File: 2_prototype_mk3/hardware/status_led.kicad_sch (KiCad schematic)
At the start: 2 parts

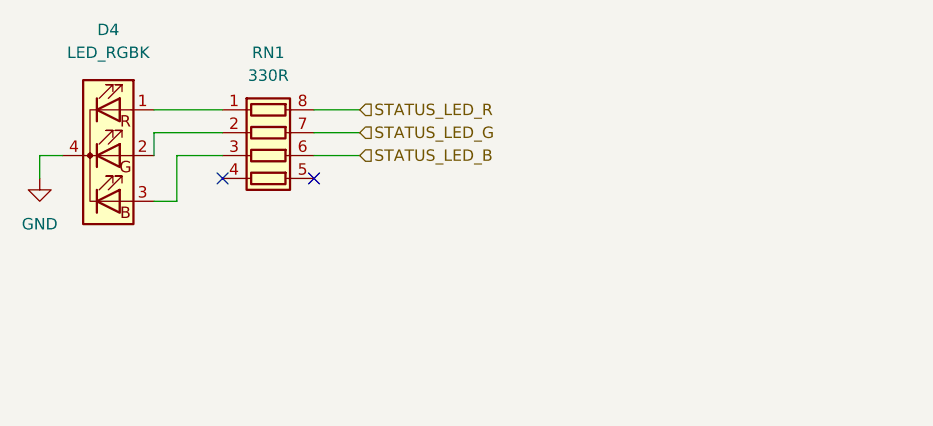
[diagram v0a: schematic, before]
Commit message: Add net classes for power
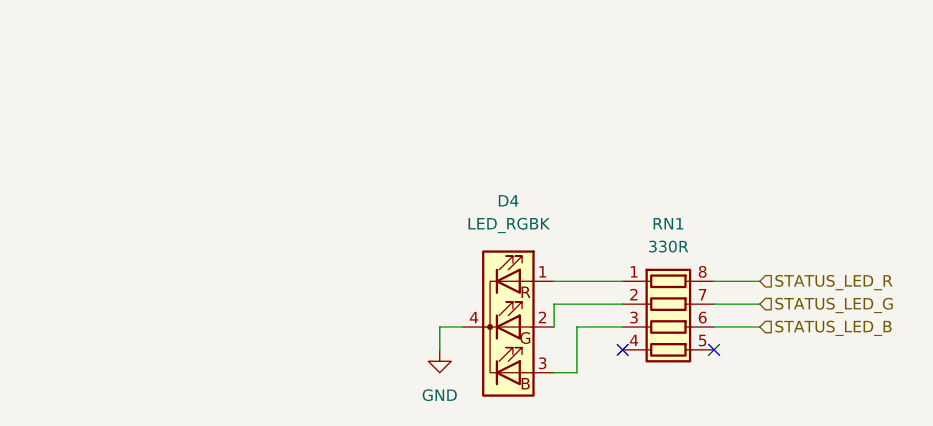
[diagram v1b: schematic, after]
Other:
- title: Status LED -> (none)
- moved on the sheet: D4, RN1
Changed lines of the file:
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@@
 	(generator "eeschema")
 	(generator_version "9.0")
-	(paper "A5")
-	(title_block
-		(title "Status LED")
-	)
+	(paper "A4")
 	(no_connect
-		(at 100.33 73.66)
+		(at 144.78 92.71)
 	)
 	(no_connect
-		(at 110.49 73.66)
-	)
-	(wire
-		(pts
-			(xy 110.49 68.58) (xy 115.57 68.58)
-		)
-		(stroke
-			(width 0)
-			(type default)
-		)
-	)
-	(wire
-		(pts
-			(xy 95.25 76.2) (xy 92.71 76.2)
-		)
-		(stroke
-			(width 0)
-			(type default)
-		)
-	)
-	(wire
-		(pts
-			(xy 100.33 71.12) (xy 95.25 71.12)
-		)
-		(stroke
-			(width 0)
-			(type default)
-		)
-	)
-	(wire
-		(pts
-			(xy 110.49 66.04) (xy 115.57 66.04)
-		)
-		(stroke
-			(width 0)
-			(type default)
-		)
-	)
-	(wire
-		(pts
-			(xy 95.25 71.12) (xy 95.25 76.2)
-		)
-		(stroke
-			(width 0)
-			(type default)
-		)
-	)
-	(wire
-		(pts
-			(xy 92.71 68.58) (xy 100.33 68.58)
-		)
-		(stroke
-			(width 0)
-			(type default)
-		)
-	)
-	(wire
-		(pts
-			(xy 80.01 71.12) (xy 80.01 73.66)
-		)
-		(stroke
-			(width 0)
-			(type default)
-		)
-	)
-	(wire
-		(pts
-			(xy 92.71 71.12) (xy 92.71 68.58)
-		)
-		(stroke
-			(width 0)
-			(type default)
-		)
-	)
-	(wire
-		(pts
-			(xy 110.49 71.12) (xy 115.57 71.12)
-		)
-		(stroke
-			(width 0)
-			(type default)
-		)
-	)
-	(wire
-		(pts
-			(xy 82.55 71.12) (xy 80.01 71.12)
-		)
-		(stroke
-			(width 0)
-			(type default)
-		)
-	)
-	(wire
-		(pts
-			(xy 92.71 66.04) (xy 100.33 66.04)
+		(at 154.94 92.71)
+	)
+	(wire
+		(pts
+			(xy 154.94 87.63) (xy 160.02 87.63)
+		)
+		(stroke
+			(width 0)
+			(type default)
+		)
+	)
+	(wire
+		(pts
+			(xy 139.7 95.25) (xy 137.16 95.25)
+		)
+		(stroke
+			(width 0)
+			(type default)
+		)
+	)
+	(wire
+		(pts
+			(xy 144.78 90.17) (xy 139.7 90.17)
+		)
+		(stroke
+			(width 0)
+			(type default)
+		)
+	)
+	(wire
+		(pts
+			(xy 154.94 85.09) (xy 160.02 85.09)
+		)
+		(stroke
+			(width 0)
+			(type default)
+		)
+	)
+	(wire
+		(pts
+			(xy 139.7 90.17) (xy 139.7 95.25)
+		)
+		(stroke
+			(width 0)
+			(type default)
+		)
+	)
+	(wire
+		(pts
+			(xy 137.16 87.63) (xy 144.78 87.63)
+		)
+		(stroke
+			(width 0)
+			(type default)
+		)
+	)
+	(wire
+		(pts
+			(xy 124.46 90.17) (xy 124.46 92.71)
+		)
+		(stroke
+			(width 0)
+			(type default)
+		)
+	)
+	(wire
+		(pts
+			(xy 137.16 90.17) (xy 137.16 87.63)
+		)
+		(stroke
+			(width 0)
+			(type default)
+		)
+	)
+	(wire
+		(pts
+			(xy 154.94 90.17) (xy 160.02 90.17)
+		)
+		(stroke
+			(width 0)
+			(type default)
+		)
+	)
+	(wire
+		(pts
+			(xy 127 90.17) (xy 124.46 90.17)
+		)
+		(stroke
+			(width 0)
+			(type default)
+		)
+	)
+	(wire
+		(pts
+			(xy 137.16 85.09) (xy 144.78 85.09)
 		)
 		(stroke
@@
 	(hierarchical_label "STATUS_LED_G"
 		(shape input)
-		(at 115.57 68.58 0)
+		(at 160.02 87.63 0)
 		(effects
 			(font
@@
 	(hierarchical_label "STATUS_LED_R"
 		(shape input)
-		(at 115.57 66.04 0)
+		(at 160.02 85.09 0)
 		(effects
 			(font
@@
 	(hierarchical_label "STATUS_LED_B"
 		(shape input)
-		(at 115.57 71.12 0)
+		(at 160.02 90.17 0)
 		(effects
 			(font
@@
 	(symbol
 		(lib_id "Device:LED_RGBK")
-		(at 87.63 71.12 0)
+		(at 132.08 90.17 0)
 		(unit 1)
 		(exclude_from_sim no)
@@
 		(fields_autoplaced yes)
 		(property "Reference" "D4"
-			(at 87.63 57.15 0)
+			(at 132.08 76.2 0)
 			(effects
 				(font
@@
 		)
 		(property "Value" "LED_RGBK"
-			(at 87.63 59.69 0)
+			(at 132.08 78.74 0)
 			(effects
 				(font
@@
 		)
 		(property "Footprint" "LED_THT:LED_D5.0mm-4_RGB"
-			(at 87.63 72.39 0)
+			(at 132.08 91.44 0)
 			(effects
 				(font
@@
 		)
 		(property "Datasheet" "~"
-			(at 87.63 72.39 0)
+			(at 132.08 91.44 0)
 			(effects
 				(font
@@
 		)
 		(property "Description" "RGB LED, red/green/blue/cathode"
-			(at 87.63 71.12 0)
+			(at 132.08 90.17 0)
 			(effects
 				(font
@@
 	(symbol
 		(lib_id "power:GND")
-		(at 80.01 73.66 0)
+		(at 124.46 92.71 0)
 		(unit 1)
 		(exclude_from_sim no)
@@
 		(fields_autoplaced yes)
 		(property "Reference" "#PWR06"
-			(at 80.01 80.01 0)
+			(at 124.46 99.06 0)
 			(effects
 				(font
@@
 		)
 		(property "Value" "GND"
-			(at 80.01 78.74 0)
+			(at 124.46 97.79 0)
 			(effects
 				(font
@@
 		)
 		(property "Footprint" ""
-			(at 80.01 73.66 0)
+			(at 124.46 92.71 0)
 			(effects
 				(font
@@
 		)
 		(property "Datasheet" ""
-			(at 80.01 73.66 0)
+			(at 124.46 92.71 0)
 			(effects
 				(font
@@
 		)
 		(property "Description" "Power symbol creates a global label with name \"GND\" , ground"
-			(at 80.01 73.66 0)
+			(at 124.46 92.71 0)
 			(effects
 				(font
@@
 	(symbol
 		(lib_id "Device:R_Pack04")
-		(at 105.41 71.12 270)
+		(at 149.86 90.17 270)
 		(unit 1)
 		(exclude_from_sim no)
@@
 		(fields_autoplaced yes)
 		(property "Reference" "RN1"
-			(at 105.41 59.69 90)
+			(at 149.86 78.74 90)
 			(effects
 				(font
@@
 		)
 		(property "Value" "330R"
-			(at 105.41 62.23 90)
+			(at 149.86 81.28 90)
 			(effects
 				(font
@@
 		)
 		(property "Footprint" "Resistor_SMD:R_Array_Convex_4x0603"
-			(at 105.41 78.105 90)
+			(at 149.86 97.155 90)
 			(effects
 				(font
@@
 		)
 		(property "Datasheet" "~"
-			(at 105.41 71.12 0)
+			(at 149.86 90.17 0)
 			(effects
 				(font
@@
 		)
 		(property "Description" "4 resistor network, parallel topology"
-			(at 105.41 71.12 0)
-			(effects
-				(font
+			(at 149.86 90.17 0)
+			(effects
+				(font

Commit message: Add manufacturer part nu bers
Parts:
- D4: Manufacturer_Part_Number (none) -> LF05RGB-01
- RN1: Manufacturer_Part_Number (none) -> YC164-JR-07330RL
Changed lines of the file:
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@@
+			)
+		)
+		(property "Manufacturer_Part_Number" "LF05RGB-01"
+			(at 132.08 90.17 0)
+			(effects
+				(font
+					(size 1.27 1.27)
+				)
+				(hide yes)
 			)
 		)
@@
 			(effects
 				(font
+					(size 1.27 1.27)
+				)
+				(hide yes)
+			)
+		)
+		(property "Manufacturer_Part_Number" "YC164-JR-07330RL"
+			(at 149.86 90.17 90)
+			(effects
+				(font
